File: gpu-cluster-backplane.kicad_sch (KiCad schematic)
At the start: 2 parts

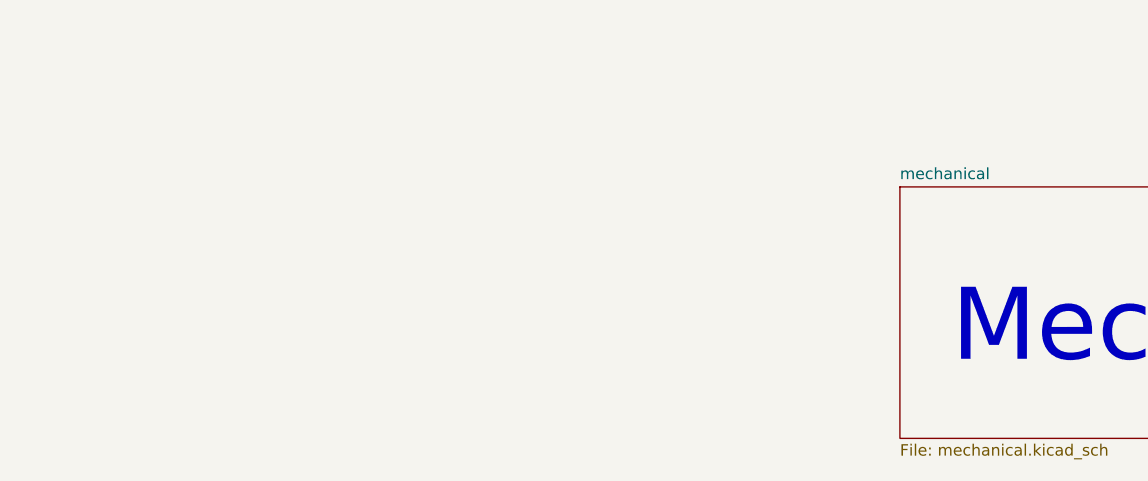
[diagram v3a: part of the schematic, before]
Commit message: Added environmental sensor to the schematic
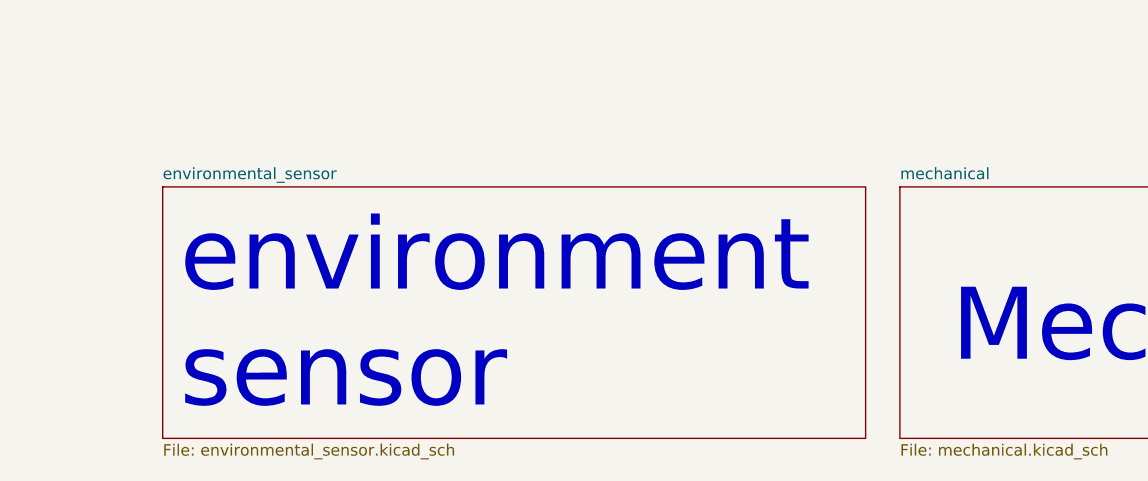
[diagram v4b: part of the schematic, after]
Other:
- added sheet environmental_sensor (environmental_sensor.kicad_sch)
- note added: "environment sensor"

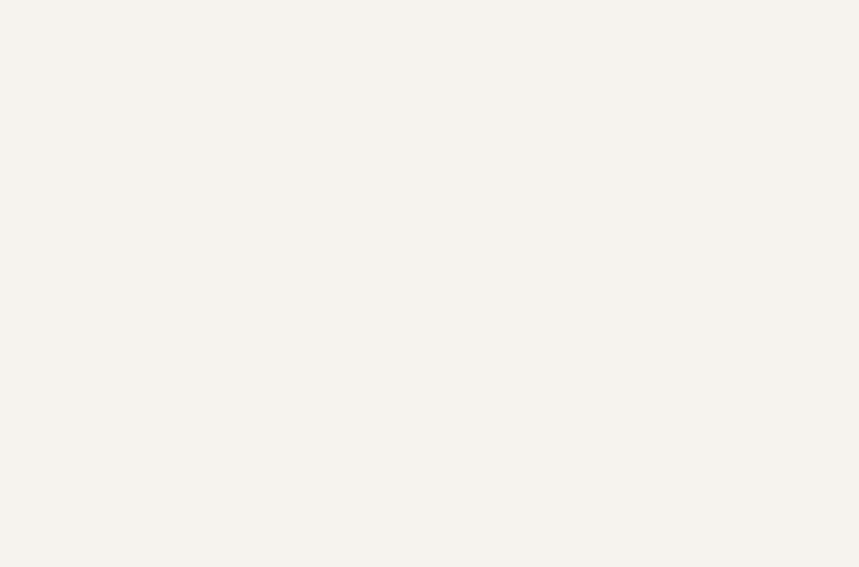
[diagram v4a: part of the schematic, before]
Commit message: Proposed arbiter for controlling fans
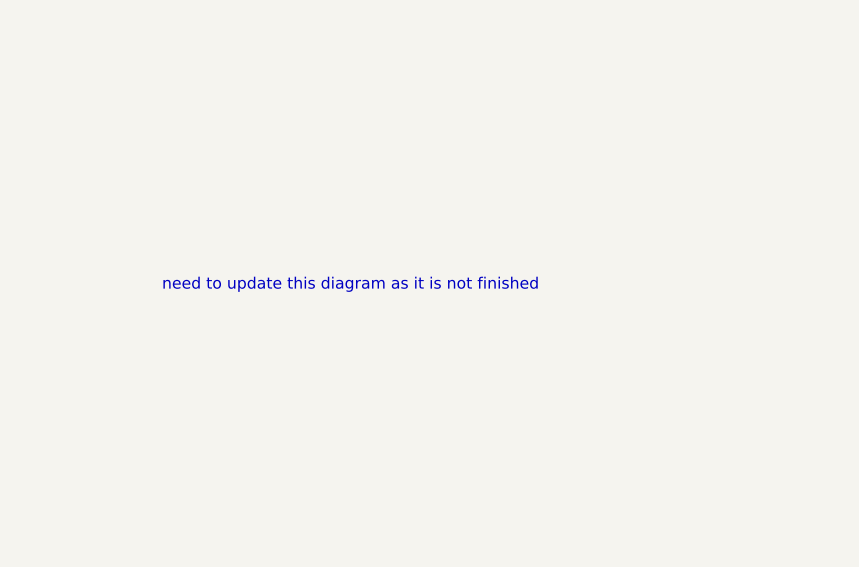
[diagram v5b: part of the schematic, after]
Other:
- note added: "need to update this diagram as it is not finished"
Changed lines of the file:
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@@
     (effects (font (size 8 8)) (justify left bottom))
+  )
+  (text "need to update this diagram as it is not finished\n"
+    (at 199.39 139.065 0)
+    (effects (font (size 1.27 1.27)) (justify left bottom))
   )
   (text "GPU Cluster Backplane" (at 15.875 23.495 0)
@@
       (reference "#PWR?") (unit 1) (value "GND") (footprint "")
     )
+    (path "/bcb16a6a-fd3f-4f16-bb24-31b44a65af30/45c15744-1f15-49d9-8ca1-fbb4faba1383"
+      (reference "#PWR?") (unit 1) (value "GND") (footprint "")
+    )
     (path "/00000000-0000-0000-0000-000062220f27/4a9ab000-5a9a-4b62-974d-a6b5c1217b3b"
       (reference "#PWR?") (unit 1) (value "GND") (footprint "")
@@
       (reference "#PWR?") (unit 1) (value "GND") (footprint "")
     )
+    (path "/bcb16a6a-fd3f-4f16-bb24-31b44a65af30/71ecbbcd-1791-4a57-90d9-0f63b4ef4912"
+      (reference "#PWR?") (unit 1) (value "GND") (footprint "")
+    )
     (path "/00000000-0000-0000-0000-000062220f27/7310497a-685c-45e6-8b16-bf1b10c01c91"
       (reference "#PWR?") (unit 1) (value "GND") (footprint "")
@@
       (reference "Q?") (unit 1) (value "2N7002K-T1-E3") (footprint "antmicro-footprints:SOT-23-3")
     )
+    (path "/bcb16a6a-fd3f-4f16-bb24-31b44a65af30/75438740-7b02-4e5d-a6d1-3a5c4e37a8f9"
+      (reference "Q?") (unit 1) (value "2N7002K-T1-E3") (footprint "antmicro-footprints:SOT-23-3")
+    )
     (path "/65998599-1c43-4f45-95a6-61fea5536bd5/d9b79d3c-2d3f-4672-a0f7-8f8fabbf71fb"
       (reference "Q?") (unit 1) (value "2N7002K-T1-E3") (footprint "antmicro-footprints:SOT-23-3")
@@
       (reference "R?") (unit 1) (value "R_10k_0402") (footprint "antmicro-footprints:R_0402_1005Metric")
     )
+    (path "/bcb16a6a-fd3f-4f16-bb24-31b44a65af30/4e7e71d9-1f5d-4377-ac51-7f69d3b41443"
+      (reference "R?") (unit 1) (value "R_10k_0402") (footprint "antmicro-footprints:R_0402_1005Metric")
+    )
     (path "/2402805b-470a-47a4-b447-56d2d6025765/4f73d459-99af-49f0-be64-ed2e694e2494"
       (reference "R?") (unit 1) (value "R_0R_0402") (footprint "antmicro-footprints:R_0402_1005Metric")
@@
       (reference "R?") (unit 1) (value "R_0R_0402") (footprint "nuc-compute-cluster-environment-sensor-footprints:R_0402_1005Metric")
     )
+    (path "/bcb16a6a-fd3f-4f16-bb24-31b44a65af30/7329a774-e62f-4251-8634-de4cee64f5ae"
+      (reference "R?") (unit 1) (value "R_10k_0402") (footprint "antmicro-footprints:R_0402_1005Metric")
+    )
     (path "/2402805b-470a-47a4-b447-56d2d6025765/75092181-0de5-4e69-89ed-c5de3766d969"
       (reference "R?") (unit 1) (value "R_10k_0402") (footprint "antmicro-footprints:R_0402_1005Metric")
@@
       (reference "U?") (unit 1) (value "FT4232H_VQFN") (footprint "nuc-compute-cluster-environment-sensor-footprints:QFN-56-1EP_8x8mm_P0.5mm")
     )
+    (path "/bcb16a6a-fd3f-4f16-bb24-31b44a65af30/0d62144d-e4c2-412b-b42b-7d6a323d2110"
+      (reference "U?") (unit 1) (value "74VHC153FT") (footprint "antmicro-footprints:TSSOP-16_4.4x5mm_P0.65mm")
+    )
     (path "/2402805b-470a-47a4-b447-56d2d6025765/0d6c2fc6-fd30-42f4-9e77-33e54c7388c6"
       (reference "U?") (unit 1) (value "TCA9534PWR") (footprint "antmicro-footprints:TSSOP-16_4.4x5mm_P0.65mm")
@@
       (reference "U?") (unit 1) (value "ADS7828") (footprint "antmicro-footprints:TSSOP-16_4.4x5mm_P0.65mm")
     )
+    (path "/bcb16a6a-fd3f-4f16-bb24-31b44a65af30/2a901979-ad99-4427-96a3-d5dc488bd67a"
+      (reference "U?") (unit 1) (value "74VHC153FT") (footprint "antmicro-footprints:TSSOP-16_4.4x5mm_P0.65mm")
+    )
     (path "/0eb7683a-233a-4366-941b-c6456024a57b/2b679113-06e9-4557-9db8-20e56580b7a8"
       (reference "U?") (unit 1) (value "SHT45") (footprint "nuc-compute-cluster-environment-sensor-footprints:Sensirion_DFN-4-1.5x1.5x0.5mm_P0.8mm")
@@
       (reference "U?") (unit 1) (value "AP62301WU-7") (footprint "d1600e-psu-breakout-board-footprints:TSOT23-6")
     )
-    (path "/00000000-0000-0000-0000-000062220f27/646a4462-16c2-4492-b1ac-5d9422cc27a3"
-      (reference "U?") (unit 1) (value "LM1117MP-25NOPB") (footprint "antmicro-footprints:SOT-223")
+    (path "/bcb16a6a-fd3f-4f16-bb24-31b44a65af30/683d8d79-59aa-46d7-a305-5f01745340d4"
+      (reference "U?") (unit 1) (value "74VHC153FT") (footprint "antmicro-footprints:TSSOP-16_4.4x5mm_P0.65mm")
     )
     (path "/8af0c60d-b845-4eae-99f7-a79a87ab7545/7aa5e833-62a3-46f0-8e03-c32d3a7a140b"
@@
       (reference "U?") (unit 1) (value "TCA9534PWR") (footprint "antmicro-footprints:TSSOP-16_4.4x5mm_P0.65mm")
     )
+    (path "/bcb16a6a-fd3f-4f16-bb24-31b44a65af30/990117c2-2bce-4681-9665-fc25a6971d95"
+      (reference "U?") (unit 1) (value "74VHC153FT") (footprint "antmicro-footprints:TSSOP-16_4.4x5mm_P0.65mm")
+    )
     (path "/8af0c60d-b845-4eae-99f7-a79a87ab7545/a3a5f7b9-a374-45e6-b4d1-007ca04ebd6c"

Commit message: Rearange hierarchical schematics
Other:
- added sheet output-control-and-data-acq (output-control.kicad_sch)
- sheet fans-control ports: added FAN_PWM_1, FAN_PWM_2, FAN_PWM_3, FAN_PWM_4, FAN_PWM_5, FAN_PWM_6, FAN_PWM_7, FAN_PWM_8; removed none
- note removed: "0"
- note removed: "environment sensor"

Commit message: Mock placement of all components on schematic
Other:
- sheet FTDI renamed FTDI-and-power
- sheet output-control-and-data-acq ports: added FAN_PWM2, FAN_PWM3, FAN_PWM4, FAN_PWM5, FAN_PWM6, FAN_PWM7, FAN_PWM8; removed none
- note added: "SignalsFromGPUs"
- note removed: "DEBUG"
- note removed: "FTDI"
- note removed: "Mechanical"
- note removed: "Y"
